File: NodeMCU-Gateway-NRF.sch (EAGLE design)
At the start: 27 parts, among them IC1 ATSHA204A, J2 GROVE-I2C, J3 Lipo Battery, J5 CON_HEADER_1X08-PTH, P1 PADSMALL, P2 PADNORMAL

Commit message: Silk error
Silk SJPWR is not tied to GPIO0 but RST/VIN
Increased SJPWR size for easy soldering
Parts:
- SJPWR: value JUMPER-PAD-3-NOYES_SILK -> JUMPER-PAD-3-2OF3_NC_BY_TRACE_LARGE; device SparkFun-Passives:JUMPER-PAD-3-NOYES_SILK -> SparkFun-Passives:JUMPER-PAD-3-2OF3_NC_BY_TRACE_LARGE
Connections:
- net SS renamed GPIO15
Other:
- note added: "Connect to Vin to put Power terminal blocks (to power board) instead of SPI OLED"
- note added: "VIN<=5V in this case mainly USB powered"
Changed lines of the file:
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@@
 <setting verticaltext="up"/>
 </settings>
-<grid distance="0.1" unitdist="inch" unit="inch" style="lines" multiple="1" display="no" altdistance="0.01" altunitdist="inch" altunit="inch"/>
+<grid distance="50" unitdist="mil" unit="mil" style="lines" multiple="1" display="yes" altdistance="5" altunitdist="mil" altunit="mil"/>
 <layers>
 <layer number="1" name="Top" color="4" fill="1" visible="no" active="no"/>
@@
 <part name="NAME" library="SparkFun-Aesthetics" deviceset="FRAME-A4L" device="" value="Value">
 <attribute name="CNAME" value="ESP8266 NodeMCU RF Gateway + Display"/>
-<attribute name="CREVISION" value="1.1"/>
+<attribute name="CREVISION" value="1.1a"/>
 <attribute name="DESIGNER" value="Charles-Henri Hallard"/>
 </part>
@@
 <part name="P+1" library="_c2h" deviceset="3V3-EXT" device="" value="3V3"/>
 <part name="VIN1" library="supply1" deviceset="+5V" device="" value="VIN"/>
-<part name="SJPWR" library="SparkFun-Passives" deviceset="JUMPER-PAD-3-NO" device="YES_SILK" value=""/>
+<part name="SJPWR" library="SparkFun-Passives" deviceset="JUMPER-PAD-3-2OF3_NC_BY_TRACE" device="_LARGE" value=""/>
 <part name="IC1" library="SparkFun-DigitalIC" deviceset="ATSHA204_SOIC8" device="" value="ATSHA204A"/>
 <part name="P+8" library="_c2h" deviceset="3V3-EXT" device="" value="3V3"/>
@@
 <text x="76.2" y="168.91" size="1.778" layer="94">LED</text>
 <text x="195.58" y="16.51" size="2.54" layer="94" font="vector" rot="MR0">File:</text>
-<text x="210.82" y="140.97" size="1.778" layer="94">SS</text>
-<text x="210.82" y="143.51" size="1.778" layer="94">FLASH</text>
-<text x="210.82" y="130.81" size="1.778" layer="94">GPIO12</text>
-<text x="210.82" y="146.05" size="1.778" layer="94">GPIO4</text>
-<text x="210.82" y="148.59" size="1.778" layer="94">GPIO5</text>
-<text x="210.82" y="123.19" size="1.778" layer="94">RXD0</text>
-<text x="210.82" y="120.65" size="1.778" layer="94">TXD0</text>
-<text x="210.82" y="128.27" size="1.778" layer="94">GPIO13</text>
-<text x="210.82" y="133.35" size="1.778" layer="94">GPIO14</text>
-<text x="210.82" y="125.73" size="1.778" layer="94">IRQ</text>
-<text x="210.82" y="151.13" size="1.778" layer="94">LED/KEY</text>
+<text x="212.09" y="140.97" size="1.778" layer="94">SS</text>
+<text x="212.09" y="143.51" size="1.778" layer="94">FLASH</text>
+<text x="212.09" y="130.81" size="1.778" layer="94">GPIO12</text>
+<text x="212.09" y="146.05" size="1.778" layer="94">GPIO4</text>
+<text x="212.09" y="148.59" size="1.778" layer="94">GPIO5</text>
+<text x="212.09" y="123.19" size="1.778" layer="94">RXD0</text>
+<text x="212.09" y="120.65" size="1.778" layer="94">TXD0</text>
+<text x="212.09" y="128.27" size="1.778" layer="94">GPIO13</text>
+<text x="212.09" y="133.35" size="1.778" layer="94">GPIO14</text>
+<text x="212.09" y="125.73" size="1.778" layer="94">IRQ</text>
+<text x="212.09" y="151.13" size="1.778" layer="94">LED/KEY</text>
 <text x="176.53" y="156.21" size="1.778" layer="94">NodeMCU Headers</text>
+<text x="95.25" y="166.37" size="1.778" layer="94">Connect to Vin to put Power
+terminal blocks (to power board)
+instead of SPI OLED</text>
+<text x="217.17" y="77.47" size="1.778" layer="94">VIN&lt;=5V in this case
+mainly USB powered</text>
 </plain>
 <instances>
@@
 </segment>
 </net>
-<net name="SS" class="0">
+<net name="GPIO15" class="0">
 <segment>
 <wire x1="209.55" y1="125.73" x2="201.93" y2="125.73" width="0.1524" layer="91"/>
-<label x="207.01" y="125.73" size="1.778" layer="95"/>
+<label x="203.2" y="125.73" size="1.778" layer="95"/>
 <pinref part="JP2" gate="G$1" pin="11"/>
 <junction x="201.93" y="125.73"/>

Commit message: Version 1.1b
NRF24L01 wiring same as mysensor gateway
Added place to add cap near NRF24L01
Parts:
- added C4: 100uF, Seeed-OPL-Discrete:CAP-POLAR-D5.3/2.0
- added SNRFIRQ: NRFIRQ, SparkFun-Passives:JUMPER-PAD-2-NOYES_SILK
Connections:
- new net N$4: RADIO1.IRQ, SNRFIRQ.1
- net 3V3: now also C4.+
- net GND: now also C4.-
- net GPIO15: now also RADIO1.CSN; no longer RADIO1.IRQ
- net GPIO16: now also SNRFIRQ.2; no longer RADIO1.CE
- net GPIO2: now also RADIO1.CE; no longer RADIO1.CSN
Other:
- note added: "IRQ RFM / CS NRF"
- note added: "SS RFM / CE NRF"
- note removed: "IRQ"
- note removed: "SS"

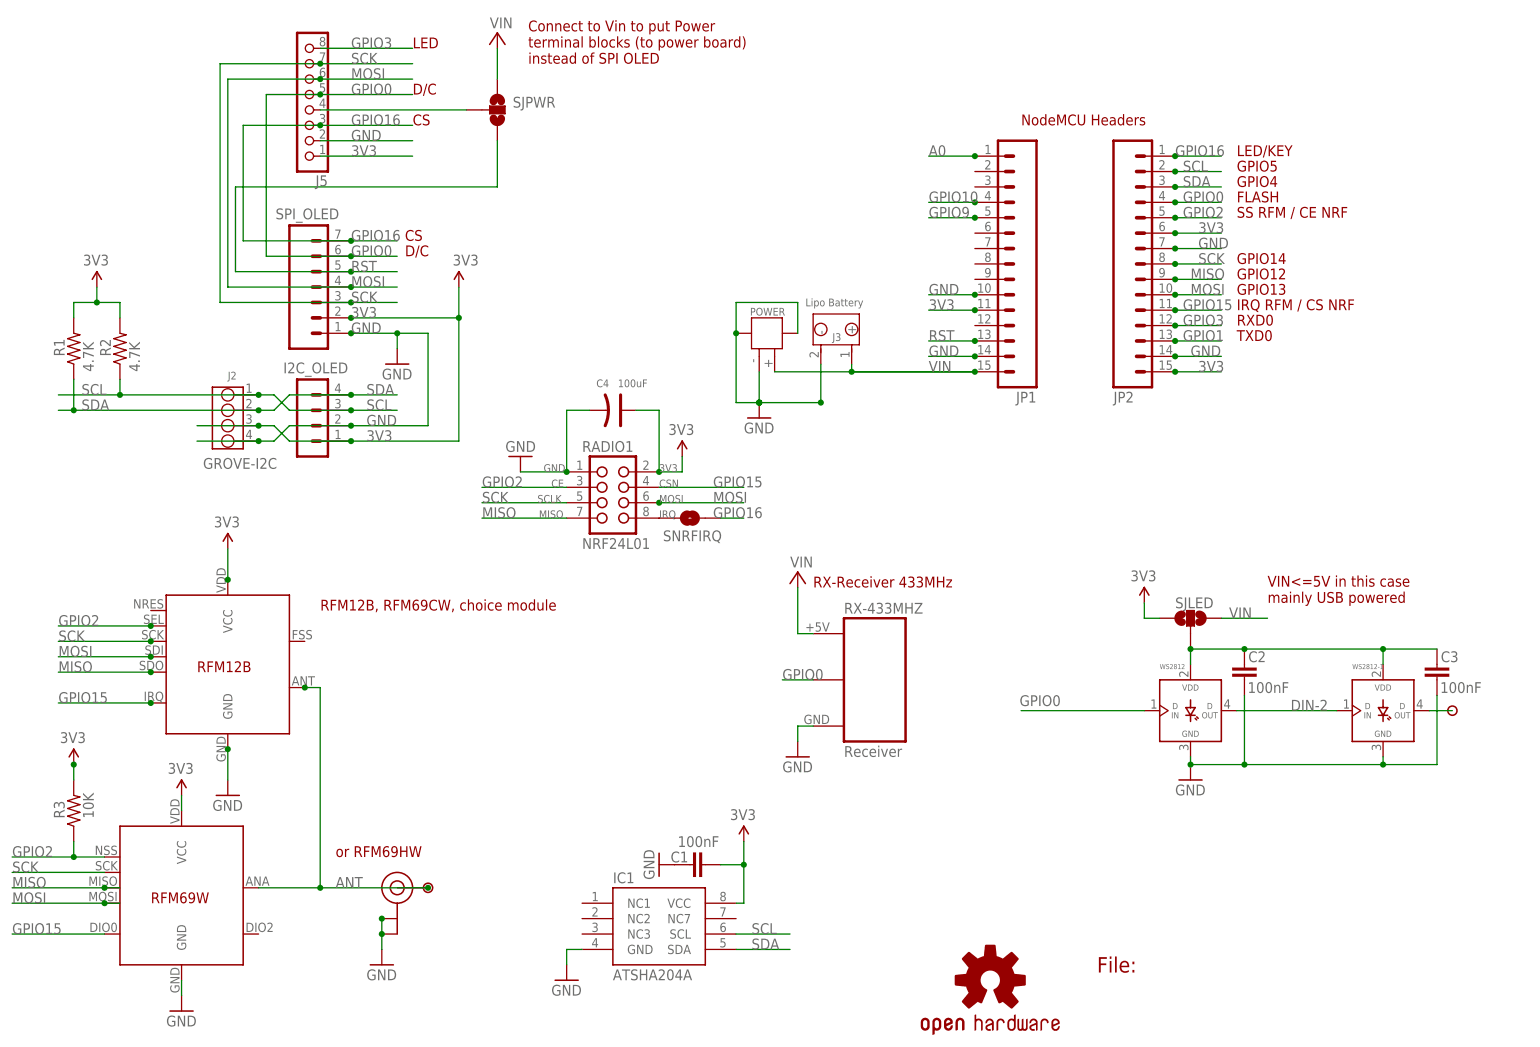
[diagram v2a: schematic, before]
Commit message: Version 1.2
Added FET to protect in case of power reverse, this avoid burning
NodeMCU board
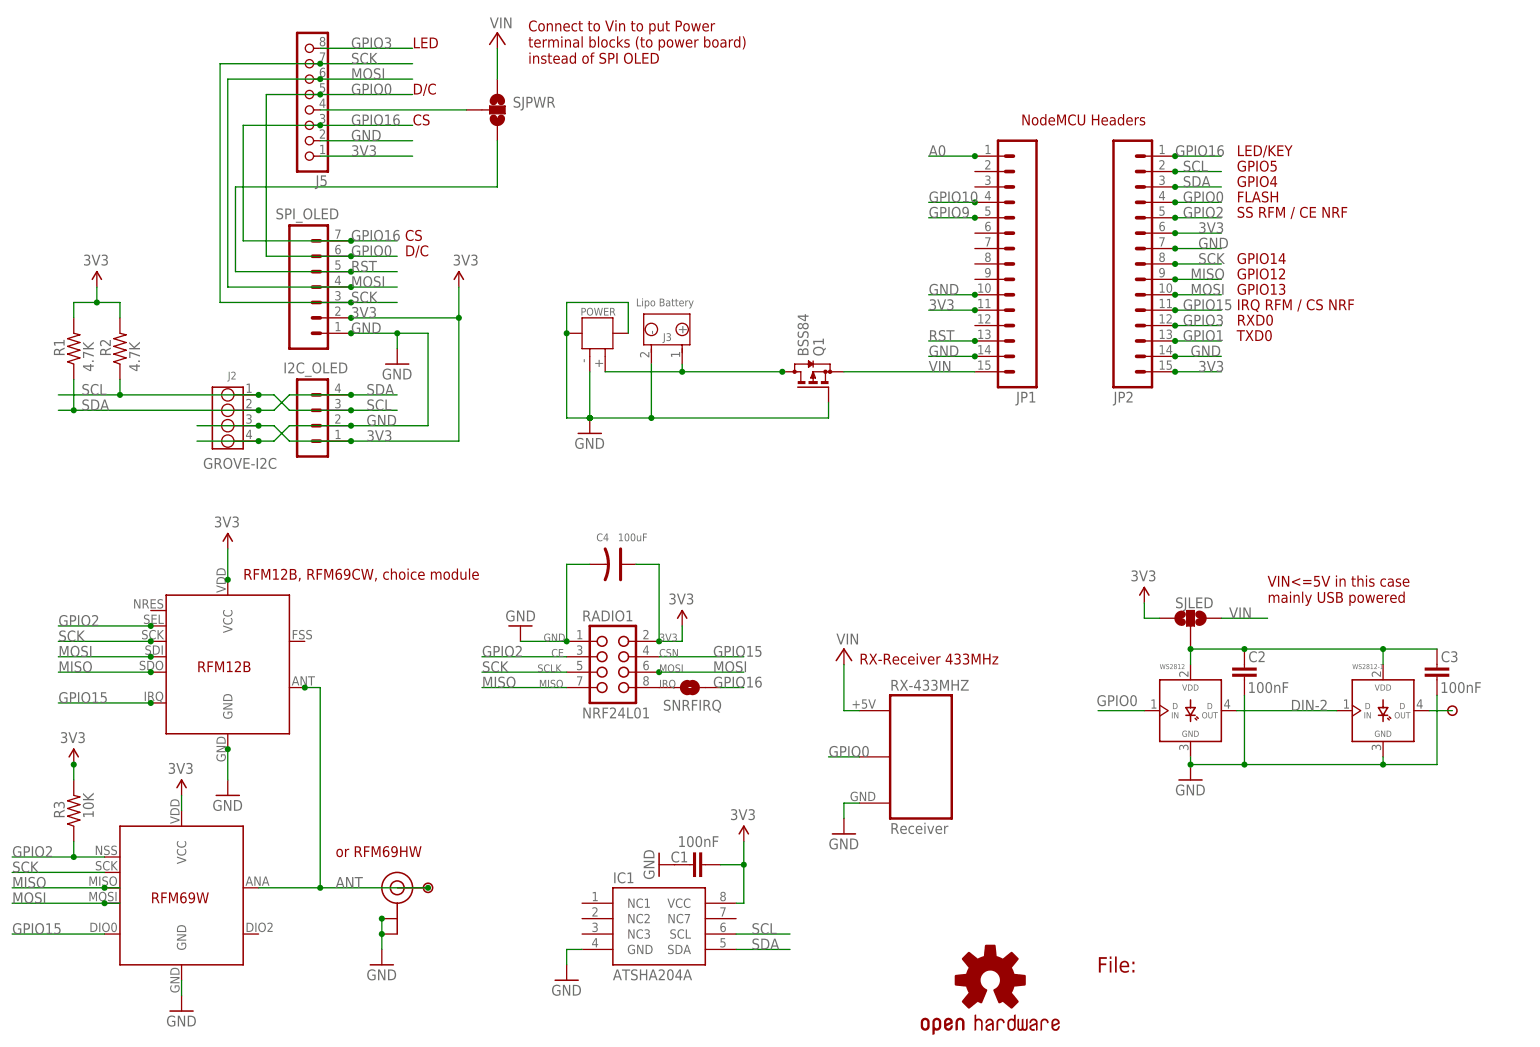
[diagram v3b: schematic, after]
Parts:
- added Q1: BSS84, transistor-small-signal:BSS84
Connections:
- new net PWR: J3.+, POWER.1, Q1.D
- net GND: now also Q1.G
- net VIN: now also Q1.S; no longer J3.+, POWER.1
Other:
- moved on the sheet: C4, J3, POWER, RADIO1, RX-433MHZ, SNRFIRQ

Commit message: Bump to V1.3
* SMA/UFL Antenna connector has been size reduced
* Antenna trace and RF Module surrounded with via for better RF
isolation
* I2C OLED connector is now "lock" version, you can just plug to test it
will fit without connector
* Increased "Isolate" ground planes to avoid shorts between connectors
and ground (may happen sometimes after soldering)
* No more LED solder pad to choose VIN/3V3, added 1N4148 diode from 5V
for the 1st LED to decrease VCC to 4.4V, always works
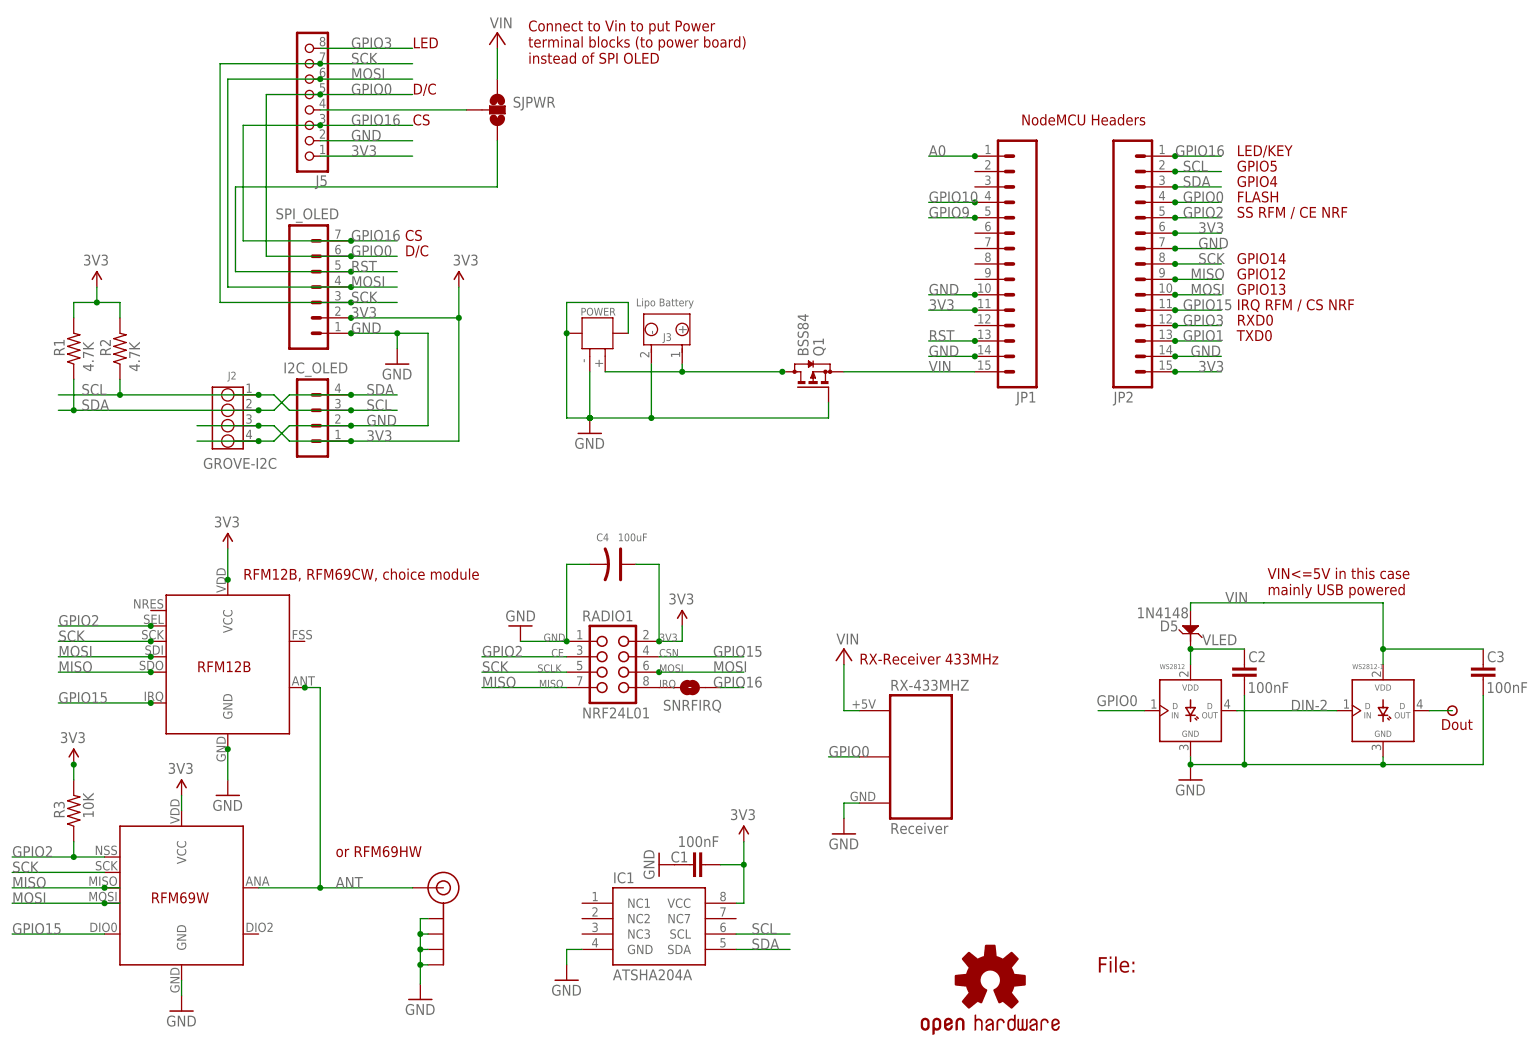
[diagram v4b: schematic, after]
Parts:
- removed P1: PADSMALL, SteveMarple:PADSMALL
- removed SJLED: JUMPER-PAD-3-2OF3_NC_BY_TRACE_LARGE, SparkFun-Passives:JUMPER-PAD-3-2OF3_NC_BY_TRACE_LARGE
- removed U-FL: U.FL, microbuilder:U.FL
- added D5: 1N4148, Seeed-Discrete:D-ESD-2P-CESD5V0D1
- added J$2: ANTENNATINY, _c2h:ANTENNATINY
- I2C_OLED: value CON_HEADER_1X04'SMALL'' -> CON_HEADER_1X04'LOCK'; device _c2h:CON_HEADER_1X04'SMALL'' -> _c2h:CON_HEADER_1X04'LOCK'
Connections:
- net 3V3: no longer SJLED.3
- net ANT: now also J$2.SIGNAL; no longer P1.1, U-FL.SIGNAL
- net GND: now also J$2.GND@0, J$2.GND@1, J$2.GND@2, J$2.GND@3; no longer U-FL.GND@0, U-FL.GND@1
- net VIN: now also C3.2, D5.1, WS2812-1.VDD; no longer SJLED.1
- net VLED: now also D5.2; no longer C3.2, SJLED.2, WS2812-1.VDD
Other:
- note added: "Dout"
- moved on the sheet: C3
